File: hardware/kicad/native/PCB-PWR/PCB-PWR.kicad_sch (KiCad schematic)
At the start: 0 parts

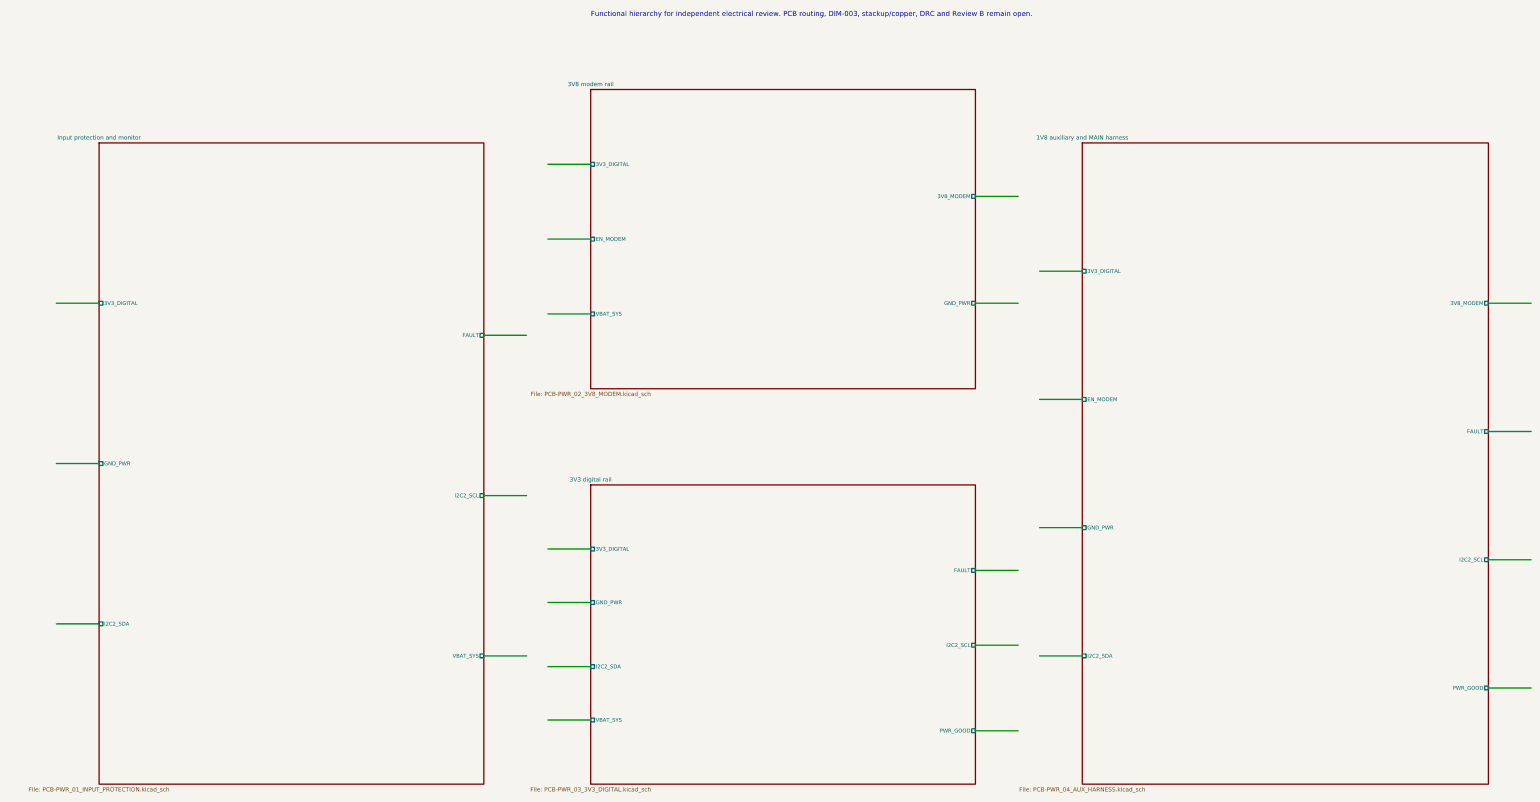
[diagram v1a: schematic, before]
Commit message: pcb-pwr: keep labels clear of connection wires
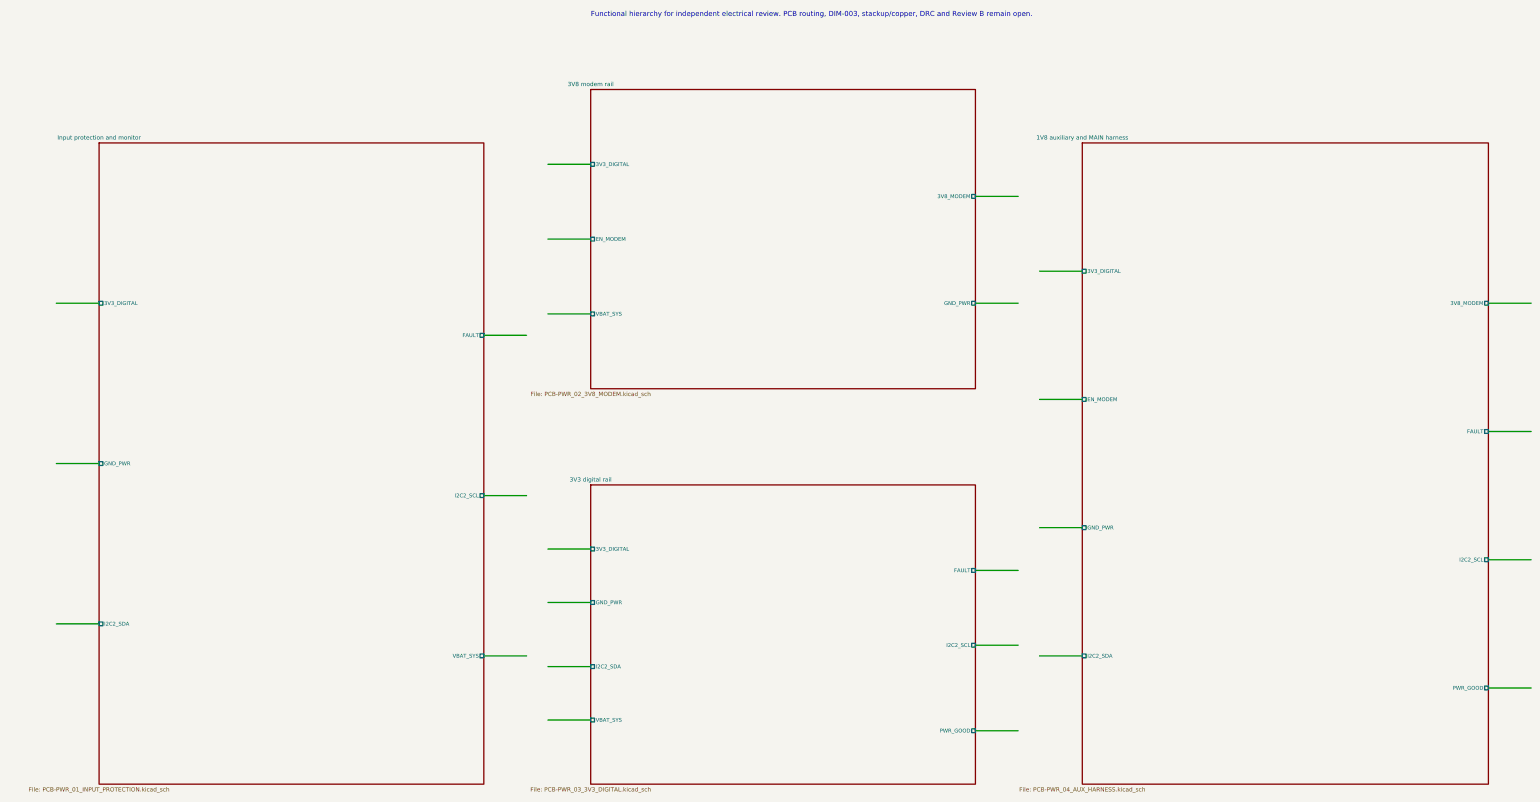
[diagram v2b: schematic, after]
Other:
- title: Dioneya EVT-PRE-20 PCB-PWR Rev.A - System overview -> PCB-PWR system overview
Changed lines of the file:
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@@
   (paper "A3")
   (title_block
-    (title "Dioneya EVT-PRE-20 PCB-PWR Rev.A - System overview")
+    (title "PCB-PWR system overview")
     (date "2026-09-17")
     (rev "A")
@@
   )
   (label "3V3_DIGITAL" (at 30.48 88.9 180)
-    (effects (font (size 0.01 0.01)) hide)
+    (effects (font (size 0.01 0.01)) (justify bottom) hide)
   )
   (label "GND_PWR" (at 30.48 127.0 180)
-    (effects (font (size 0.01 0.01)) hide)
+    (effects (font (size 0.01 0.01)) (justify bottom) hide)
   )
   (label "I2C2_SDA" (at 30.48 165.1 180)
-    (effects (font (size 0.01 0.01)) hide)
+    (effects (font (size 0.01 0.01)) (justify bottom) hide)
   )
   (label "FAULT" (at 142.24 96.52 0)
-    (effects (font (size 0.01 0.01)) hide)
+    (effects (font (size 0.01 0.01)) (justify bottom) hide)
   )
   (label "I2C2_SCL" (at 142.24 134.62 0)
-    (effects (font (size 0.01 0.01)) hide)
+    (effects (font (size 0.01 0.01)) (justify bottom) hide)
   )
   (label "VBAT_SYS" (at 142.24 172.72 0)
-    (effects (font (size 0.01 0.01)) hide)
+    (effects (font (size 0.01 0.01)) (justify bottom) hide)
   )
   (label "3V3_DIGITAL" (at 147.32 55.88 180)
-    (effects (font (size 0.01 0.01)) hide)
+    (effects (font (size 0.01 0.01)) (justify bottom) hide)
   )
   (label "EN_MODEM" (at 147.32 73.66 180)
-    (effects (font (size 0.01 0.01)) hide)
+    (effects (font (size 0.01 0.01)) (justify bottom) hide)
   )
   (label "VBAT_SYS" (at 147.32 91.44 180)
-    (effects (font (size 0.01 0.01)) hide)
+    (effects (font (size 0.01 0.01)) (justify bottom) hide)
   )
   (label "3V8_MODEM" (at 259.08 63.5 0)
-    (effects (font (size 0.01 0.01)) hide)
+    (effects (font (size 0.01 0.01)) (justify bottom) hide)
   )
   (label "GND_PWR" (at 259.08 88.9 0)
-    (effects (font (size 0.01 0.01)) hide)
+    (effects (font (size 0.01 0.01)) (justify bottom) hide)
   )
   (label "3V3_DIGITAL" (at 147.32 147.32 180)
-    (effects (font (size 0.01 0.01)) hide)
+    (effects (font (size 0.01 0.01)) (justify bottom) hide)
   )
   (label "GND_PWR" (at 147.32 160.02 180)
-    (effects (font (size 0.01 0.01)) hide)
+    (effects (font (size 0.01 0.01)) (justify bottom) hide)
   )
   (label "I2C2_SDA" (at 147.32 175.26 180)
-    (effects (font (size 0.01 0.01)) hide)
+    (effects (font (size 0.01 0.01)) (justify bottom) hide)
   )
   (label "VBAT_SYS" (at 147.32 187.96 180)
-    (effects (font (size 0.01 0.01)) hide)
+    (effects (font (size 0.01 0.01)) (justify bottom) hide)
   )
   (label "FAULT" (at 259.08 152.4 0)
-    (effects (font (size 0.01 0.01)) hide)
+    (effects (font (size 0.01 0.01)) (justify bottom) hide)
   )
   (label "I2C2_SCL" (at 259.08 170.18 0)
-    (effects (font (size 0.01 0.01)) hide)
+    (effects (font (size 0.01 0.01)) (justify bottom) hide)
   )
   (label "PWR_GOOD" (at 259.08 190.5 0)
-    (effects (font (size 0.01 0.01)) hide)
+    (effects (font (size 0.01 0.01)) (justify bottom) hide)
   )
   (label "3V3_DIGITAL" (at 264.16 81.28 180)
-    (effects (font (size 0.01 0.01)) hide)
+    (effects (font (size 0.01 0.01)) (justify bottom) hide)
   )
   (label "EN_MODEM" (at 264.16 111.76 180)
-    (effects (font (size 0.01 0.01)) hide)
+    (effects (font (size 0.01 0.01)) (justify bottom) hide)
   )
   (label "GND_PWR" (at 264.16 142.24 180)
-    (effects (font (size 0.01 0.01)) hide)
+    (effects (font (size 0.01 0.01)) (justify bottom) hide)
   )
   (label "I2C2_SDA" (at 264.16 172.72 180)
-    (effects (font (size 0.01 0.01)) hide)
+    (effects (font (size 0.01 0.01)) (justify bottom) hide)
   )
   (label "3V8_MODEM" (at 381.0 88.9 0)
-    (effects (font (size 0.01 0.01)) hide)
+    (effects (font (size 0.01 0.01)) (justify bottom) hide)
   )
   (label "FAULT" (at 381.0 119.38 0)
-    (effects (font (size 0.01 0.01)) hide)
+    (effects (font (size 0.01 0.01)) (justify bottom) hide)
   )
   (label "I2C2_SCL" (at 381.0 149.86 0)
-    (effects (font (size 0.01 0.01)) hide)
+    (effects (font (size 0.01 0.01)) (justify bottom) hide)
   )
   (label "PWR_GOOD" (at 381.0 180.34 0)
-    (effects (font (size 0.01 0.01)) hide)
+    (effects (font (size 0.01 0.01)) (justify bottom) hide)
   )
   (sheet (at 40.64 50.8) (size 91.44 152.4)
@@
     )
     (pin "3V3_DIGITAL" passive (at 40.64 88.9 180)
-      (effects (font (size 0.9 0.9)))
+      (effects (font (size 0.9 0.9)) (justify bottom))
     )
     (pin "GND_PWR" passive (at 40.64 127.0 180)
-      (effects (font (size 0.9 0.9)))
+      (effects (font (size 0.9 0.9)) (justify bottom))
     )
     (pin "I2C2_SDA" passive (at 40.64 165.1 180)
-      (effects (font (size 0.9 0.9)))
+      (effects (font (size 0.9 0.9)) (justify bottom))
     )
     (pin "FAULT" passive (at 132.07999999999998 96.52 0)
-      (effects (font (size 0.9 0.9)))
+      (effects (font (size 0.9 0.9)) (justify bottom))
     )
     (pin "I2C2_SCL" passive (at 132.07999999999998 134.62 0)
-      (effects (font (size 0.9 0.9)))
+      (effects (font (size 0.9 0.9)) (justify bottom))
     )
     (pin "VBAT_SYS" passive (at 132.07999999999998 172.72 0)
-      (effects (font (size 0.9 0.9)))
+      (effects (font (size 0.9 0.9)) (justify bottom))
     )
     (instances
@@
     )
     (pin "3V3_DIGITAL" passive (at 157.48 55.88 180)
-      (effects (font (size 0.9 0.9)))
+      (effects (font (size 0.9 0.9)) (justify bottom))
     )
     (pin "EN_MODEM" passive (at 157.48 73.66 180)
-      (effects (font (size 0.9 0.9)))
+      (effects (font (size 0.9 0.9)) (justify bottom))
     )
     (pin "VBAT_SYS" passive (at 157.48 91.44 180)
-      (effects (font (size 0.9 0.9)))
+      (effects (font (size 0.9 0.9)) (justify bottom))
     )
     (pin "3V8_MODEM" passive (at 248.92 63.5 0)
-      (effects (font (size 0.9 0.9)))
+      (effects (font (size 0.9 0.9)) (justify bottom))
     )
     (pin "GND_PWR" passive (at 248.92 88.9 0)
-      (effects (font (size 0.9 0.9)))
+      (effects (font (size 0.9 0.9)) (justify bottom))
     )
     (instances
@@
     )
     (pin "3V3_DIGITAL" passive (at 157.48 147.32 180)
-      (effects (font (size 0.9 0.9)))
+      (effects (font (size 0.9 0.9)) (justify bottom))
     )
     (pin "GND_PWR" passive (at 157.48 160.02 180)
-      (effects (font (size 0.9 0.9)))
+      (effects (font (size 0.9 0.9)) (justify bottom))
     )
     (pin "I2C2_SDA" passive (at 157.48 175.26 180)
-      (effects (font (size 0.9 0.9)))
+      (effects (font (size 0.9 0.9)) (justify bottom))
     )
     (pin "VBAT_SYS" passive (at 157.48 187.96 180)
-      (effects (font (size 0.9 0.9)))
+      (effects (font (size 0.9 0.9)) (justify bottom))
     )
     (pin "FAULT" passive (at 248.92 152.4 0)
-      (effects (font (size 0.9 0.9)))
+      (effects (font (size 0.9 0.9)) (justify bottom))
     )
     (pin "I2C2_SCL" passive (at 248.92 170.18 0)
-      (effects (font (size 0.9 0.9)))
+      (effects (font (size 0.9 0.9)) (justify bottom))
     )
     (pin "PWR_GOOD" passive (at 248.92 190.5 0)
-      (effects (font (size 0.9 0.9)))
+      (effects (font (size 0.9 0.9)) (justify bottom))
     )
     (instances
@@
     )
     (pin "3V3_DIGITAL" passive (at 274.32 81.28 180)
-      (effects (font (size 0.9 0.9)))
+      (effects (font (size 0.9 0.9)) (justify bottom))
     )
     (pin "EN_MODEM" passive (at 274.32 111.76 180)
-      (effects (font (size 0.9 0.9)))
+      (effects (font (size 0.9 0.9)) (justify bottom))
     )
     (pin "GND_PWR" passive (at 274.32 142.24 180)
-      (effects (font (size 0.9 0.9)))
+      (effects (font (size 0.9 0.9)) (justify bottom))
     )
     (pin "I2C2_SDA" passive (at 274.32 172.72 180)
-      (effects (font (size 0.9 0.9)))
+      (effects (font (size 0.9 0.9)) (justify bottom))
     )
     (pin "3V8_MODEM" passive (at 370.84 88.9 0)
-      (effects (font (size 0.9 0.9)))
+      (effects (font (size 0.9 0.9)) (justify bottom))
     )
     (pin "FAULT" passive (at 370.84 119.38 0)
-      (effects (font (size 0.9 0.9)))
+      (effects (font (size 0.9 0.9)) (justify bottom))
     )
     (pin "I2C2_SCL" passive (at 370.84 149.86 0)
-      (effects (font (size 0.9 0.9)))
+      (effects (font (size 0.9 0.9)) (justify bottom))
     )
     (pin "PWR_GOOD" passive (at 370.84 180.34 0)
-      (effects (font (size 0.9 0.9)))
+      (effects (font (size 0.9 0.9)) (justify bottom))
     )
     (instances
